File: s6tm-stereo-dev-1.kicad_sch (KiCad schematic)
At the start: 95 parts, among them J1 Micro_SD_Card_Det1, J2 Conn_01x04_Pin, J3 USB_C_Receptacle_USB2.0_14P, SW1 SW_SPDT, SW2 SW_Push, SW3 SW_Push, SW5 SW_Push, SW6 SW_Push, SW7 RotaryEncoder_Switch, U1 ESP32-S3FN8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

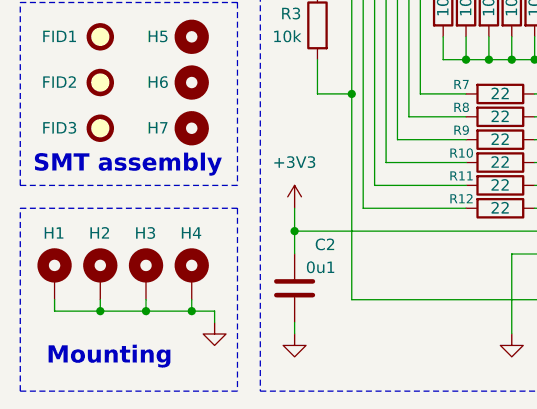
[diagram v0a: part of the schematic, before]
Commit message: schem/pcb: remove extra mounting hole
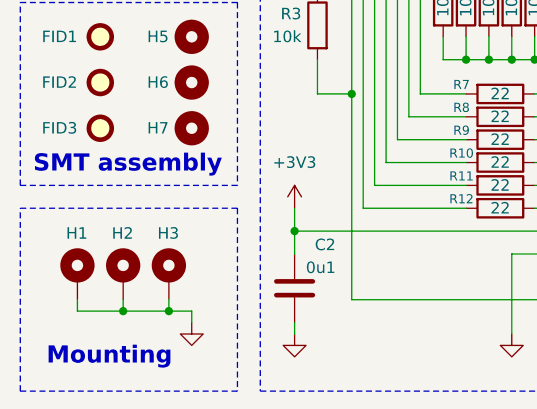
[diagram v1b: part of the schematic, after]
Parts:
- removed H4: MountingHole_Pad, MountingHole:MountingHole_3.2mm_M3_Pad_Via, symbol Mechanical:MountingHole_Pad
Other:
- moved on the sheet: H1, H2, H3
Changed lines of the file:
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@@
 	)
 	(junction
-		(at 29.21 185.42)
-		(diameter 0)
-		(color 0 0 0 0)
-	)
-	(junction
 		(at 64.77 157.48)
 		(diameter 0)
@@
 	)
 	(junction
-		(at 24.13 185.42)
-		(diameter 0)
-		(color 0 0 0 0)
-	)
-	(junction
 		(at 58.42 144.78)
 		(diameter 0)
@@
 	)
 	(junction
+		(at 31.75 185.42)
+		(diameter 0)
+		(color 0 0 0 0)
+	)
+	(junction
 		(at 153.67 180.34)
 		(diameter 0)
@@
 	)
 	(junction
-		(at 54.61 31.75)
+		(at 26.67 185.42)
 		(diameter 0)
 		(color 0 0 0 0)
 	)
 	(junction
-		(at 195.58 124.46)
+		(at 54.61 31.75)
 		(diameter 0)
 		(color 0 0 0 0)
 	)
 	(junction
-		(at 59.69 146.05)
+		(at 195.58 124.46)
 		(diameter 0)
 		(color 0 0 0 0)
 	)
 	(junction
-		(at 34.29 185.42)
+		(at 59.69 146.05)
 		(diameter 0)
 		(color 0 0 0 0)
@@
 	(wire
 		(pts
+			(xy 31.75 185.42) (xy 34.29 185.42)
+		)
+		(stroke
+			(width 0)
+			(type default)
+		)
+	)
+	(wire
+		(pts
 			(xy 67.31 143.51) (xy 57.15 143.51)
 		)
@@
 	(wire
 		(pts
-			(xy 19.05 185.42) (xy 24.13 185.42)
+			(xy 21.59 185.42) (xy 26.67 185.42)
 		)
 		(stroke
@@
 	(wire
 		(pts
-			(xy 19.05 185.42) (xy 19.05 184.15)
+			(xy 21.59 185.42) (xy 21.59 184.15)
 		)
 		(stroke
@@
 	(wire
 		(pts
-			(xy 29.21 185.42) (xy 29.21 184.15)
+			(xy 31.75 185.42) (xy 31.75 184.15)
 		)
 		(stroke
@@
 	(wire
 		(pts
-			(xy 34.29 185.42) (xy 34.29 184.15)
-		)
-		(stroke
-			(width 0)
-			(type default)
-		)
-	)
-	(wire
-		(pts
 			(xy 153.67 71.12) (xy 153.67 72.39)
 		)
@@
 	(wire
 		(pts
-			(xy 36.83 185.42) (xy 34.29 185.42)
-		)
-		(stroke
-			(width 0)
-			(type default)
-		)
-	)
-	(wire
-		(pts
 			(xy 77.47 21.59) (xy 78.74 21.59)
 		)
@@
 	(wire
 		(pts
-			(xy 24.13 185.42) (xy 29.21 185.42)
-		)
-		(stroke
-			(width 0)
-			(type default)
-		)
-	)
-	(wire
-		(pts
 			(xy 72.39 154.94) (xy 72.39 157.48)
 		)
@@
 	(wire
 		(pts
+			(xy 26.67 185.42) (xy 31.75 185.42)
+		)
+		(stroke
+			(width 0)
+			(type default)
+		)
+	)
+	(wire
+		(pts
 			(xy 195.58 119.38) (xy 195.58 124.46)
 		)
@@
 	(wire
 		(pts
-			(xy 29.21 185.42) (xy 34.29 185.42)
-		)
-		(stroke
-			(width 0)
-			(type default)
-		)
-	)
-	(wire
-		(pts
 			(xy 250.19 147.32) (xy 252.73 147.32)
 		)
@@
 	(wire
 		(pts
-			(xy 36.83 185.42) (xy 36.83 186.69)
+			(xy 34.29 185.42) (xy 34.29 186.69)
 		)
 		(stroke
@@
 	(wire
 		(pts
-			(xy 24.13 185.42) (xy 24.13 184.15)
+			(xy 26.67 185.42) (xy 26.67 184.15)
 		)
 		(stroke
@@
 	(symbol
 		(lib_id "Mechanical:MountingHole_Pad")
-		(at 29.21 181.61 0)
+		(at 31.75 181.61 0)
 		(unit 1)
 		(body_style 1)
@@
 		(dnp no)
 		(property "Reference" "H3"
-			(at 27.94 176.784 0)
+			(at 30.48 176.784 0)
 			(show_name no)
 			(do_not_autoplace no)
@@
 		)
 		(property "Value" "MountingHole_Pad"
-			(at 33.02 180.34 90)
+			(at 35.56 180.34 90)
 			(hide yes)
 			(show_name no)
@@
 		)
 		(property "Footprint" "MountingHole:MountingHole_3.2mm_M3_Pad_Via"
-			(at 29.21 181.61 0)
+			(at 31.75 181.61 0)
 			(hide yes)
 			(show_name no)
@@
 		)
 		(property "Datasheet" ""
-			(at 29.21 181.61 0)
+			(at 31.75 181.61 0)
 			(hide yes)
 			(show_name no)
@@
 		)
 		(property "Description" "Mounting Hole with connection"
-			(at 29.21 181.61 0)
+			(at 31.75 181.61 0)
 			(hide yes)
 			(show_name no)
@@
 	(symbol
 		(lib_id "power:GND")
-		(at 36.83 186.69 0)
+		(at 34.29 186.69 0)
 		(unit 1)
 		(body_style 1)
@@
 		(dnp no)
 		(property "Reference" "#PWR0126"
-			(at 36.83 193.04 0)
+			(at 34.29 193.04 0)
 			(hide yes)
 			(show_name no)
@@
 		)
 		(property "Value" "GND"
-			(at 36.576 191.262 0)
+			(at 34.036 191.262 0)
 			(hide yes)
 			(show_name no)
@@
 		)
 		(property "Footprint" ""
-			(at 36.83 186.69 0)
+			(at 34.29 186.69 0)
 			(hide yes)
 			(show_name no)
@@
 		)
 		(property "Datasheet" ""
-			(at 36.83 186.69 0)
+			(at 34.29 186.69 0)
 			(hide yes)
 			(show_name no)
@@
 		)
 		(property "Description" "Power symbol creates a global label with name \"GND\" , ground"
-			(at 36.83 186.69 0)
+			(at 34.29 186.69 0)
 			(hide yes)
 			(show_name no)
@@
 	)
 	(symbol
-		(lib_id "Mechanical:MountingHole_Pad")
-		(at 34.29 181.61 0)
-		(unit 1)
-		(body_style 1)
-		(exclude_from_sim no)
-		(in_bom no)
-		(on_board yes)
-		(in_pos_files yes)
-		(dnp no)
-		(property "Reference" "H4"
-			(at 33.02 176.784 0)
-			(show_name no)
-			(do_not_autoplace no)
-			(effects
-				(font
-					(size 1.27 1.27)
-				)
-				(justify left)
-			)
-		)
-		(property "Value" "MountingHole_Pad"
-			(at 38.1 180.34 90)
-			(hide yes)
-			(show_name no)
-			(do_not_autoplace no)
-			(effects
-				(font
-					(size 1.27 1.27)
-				)
-			)
-		)
-		(property "Footprint" "MountingHole:MountingHole_3.2mm_M3_Pad_Via"
-			(at 34.29 181.61 0)
-			(hide yes)
-			(show_name no)
-			(do_not_autoplace no)
-			(effects
-				(font
-					(size 1.27 1.27)
-				)
-			)
-		)
-		(property "Datasheet" ""
-			(at 34.29 181.61 0)
-			(hide yes)
-			(show_name no)
-			(do_not_autoplace no)
-			(effects
-				(font
-					(size 1.27 1.27)
-				)
-			)
-		)
-		(property "Description" "Mounting Hole with connection"
-			(at 34.29 181.61 0)
-			(hide yes)
-			(show_name no)
-			(do_not_autoplace no)
-			(effects
-				(font
-					(size 1.27 1.27)
-				)
-			)
-		)
-		(pin "1"
-		)
-		(instances
-			(project "s6tm-stereo-dev-1"
-				(path "/41fad0d7-0cae-453e-a16c-bdf8be036e99"
-					(reference "H4")
-					(unit 1)
-				)
-			)
-		)
-	)
-	(symbol
 		(lib_id "Device:D_Schottky")
 		(at 270.51 127 0)
@@
 	(symbol
 		(lib_id "Mechanical:MountingHole_Pad")
-		(at 24.13 181.61 0)
+		(at 26.67 181.61 0)
 		(unit 1)
 		(body_style 1)
@@
 		(dnp no)
 		(property "Reference" "H2"
-			(at 22.86 176.784 0)
+			(at 25.4 176.784 0)
 			(show_name no)
 			(do_not_autoplace no)
@@
 		)
 		(property "Value" "MountingHole_Pad"
-			(at 27.94 180.34 90)
+			(at 30.48 180.34 90)
 			(hide yes)
 			(show_name no)
@@
 		)
 		(property "Footprint" "MountingHole:MountingHole_3.2mm_M3_Pad_Via"
-			(at 24.13 181.61 0)
+			(at 26.67 181.61 0)
 			(hide yes)
 			(show_name no)
@@
 		)
 		(property "Datasheet" ""
-			(at 24.13 181.61 0)
+			(at 26.67 181.61 0)
 			(hide yes)
 			(show_name no)
@@
 		)
 		(property "Description" "Mounting Hole with connection"
-			(at 24.13 181.61 0)
+			(at 26.67 181.61 0)
 			(hide yes)
 			(show_name no)
@@
 	(symbol
 		(lib_id "Mechanical:MountingHole_Pad")
-		(at 19.05 181.61 0)
+		(at 21.59 181.61 0)
 		(unit 1)
 		(body_style 1)
@@
 		(dnp no)
 		(property "Reference" "H1"
-			(at 17.78 176.784 0)
+			(at 20.32 176.784 0)
 			(show_name no)
 			(do_not_autoplace no)
@@
 		)
 		(property "Value" "MountingHole_Pad"
-			(at 22.86 180.34 90)
+			(at 25.4 180.34 90)
 			(hide yes)
 			(show_name no)
@@
 		)
 		(property "Footprint" "MountingHole:MountingHole_3.2mm_M3_Pad_Via"
-			(at 19.05 181.61 0)
+			(at 21.59 181.61 0)
 			(hide yes)
 			(show_name no)
@@
 		)
 		(property "Datasheet" ""
-			(at 19.05 181.61 0)
+			(at 21.59 181.61 0)
 			(hide yes)
 			(show_name no)
@@
 		)
 		(property "Description" "Mounting Hole with connection"
-			(at 19.05 181.61 0)
+			(at 21.59 181.61 0)
 			(hide yes)
 			(show_name no)

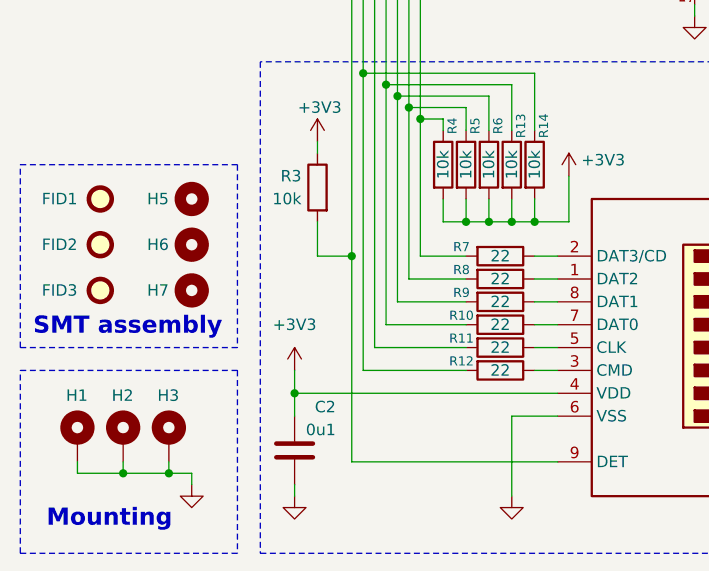
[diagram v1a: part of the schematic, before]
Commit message: pcb: refine sd layout
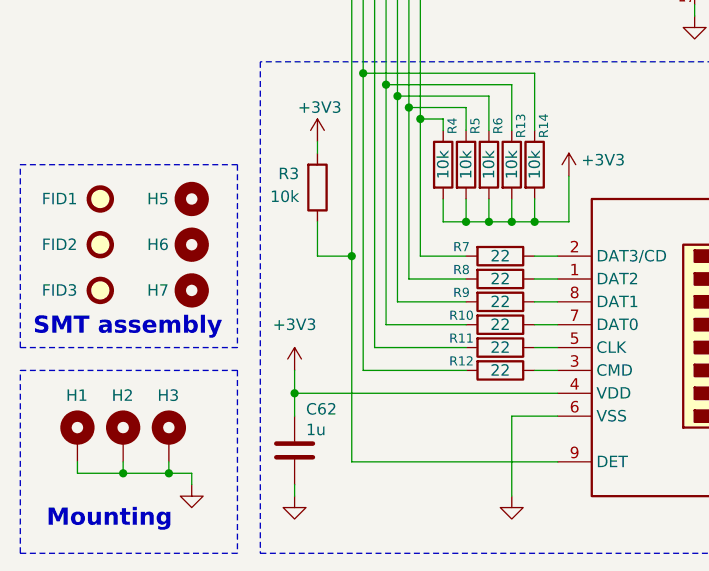
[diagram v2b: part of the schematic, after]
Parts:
- removed C2: 0u1, Capacitor_SMD:C_0603_1608Metric, symbol Device:C
- added C62: 1u, Capacitor_SMD:C_0402_1005Metric, symbol Device:C
- R3: footprint Resistor_SMD:R_0603_1608Metric -> Resistor_SMD:R_0402_1005Metric; JLCPCB Part # C25804 -> C25744; Manufacturer Part Number 0603WAF1002T5E -> 0402WGF1002TCE
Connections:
- net +3V3: now also R3.2, C62.1; no longer R3.1
- net GND: now also C62.2
- net at J1.9 (DET), U1.36 (SPICLK_N/GPIO48): now also R3.1; no longer R3.2

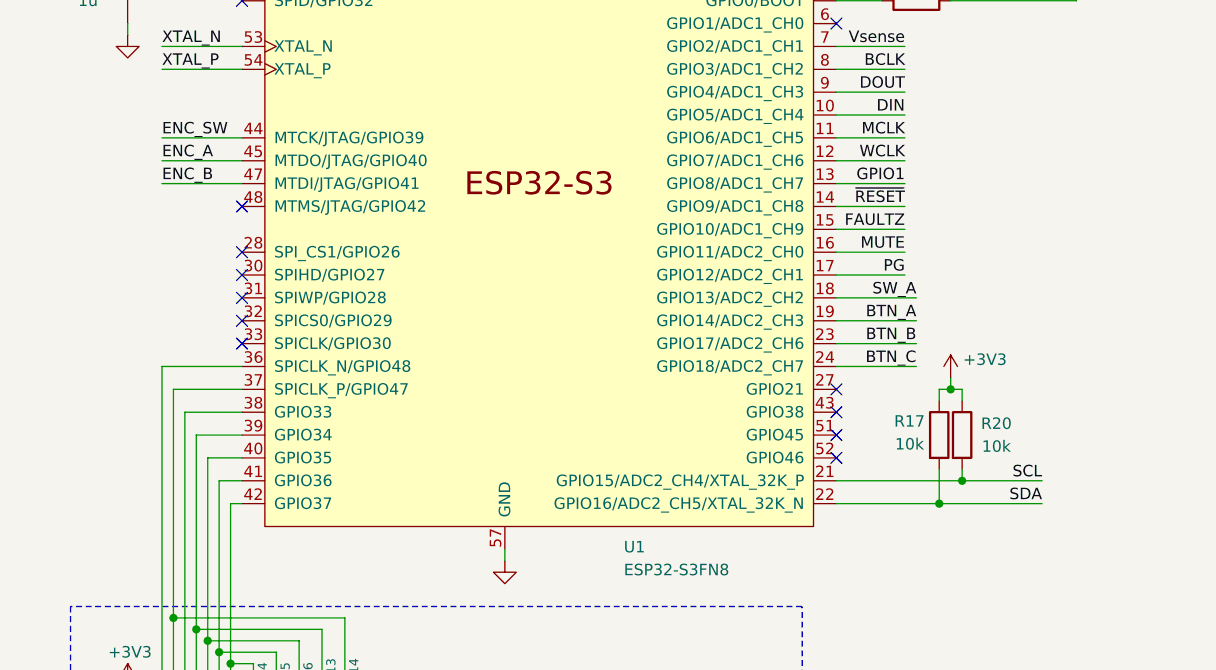
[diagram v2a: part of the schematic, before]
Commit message: pcb: add HSE xtal routing
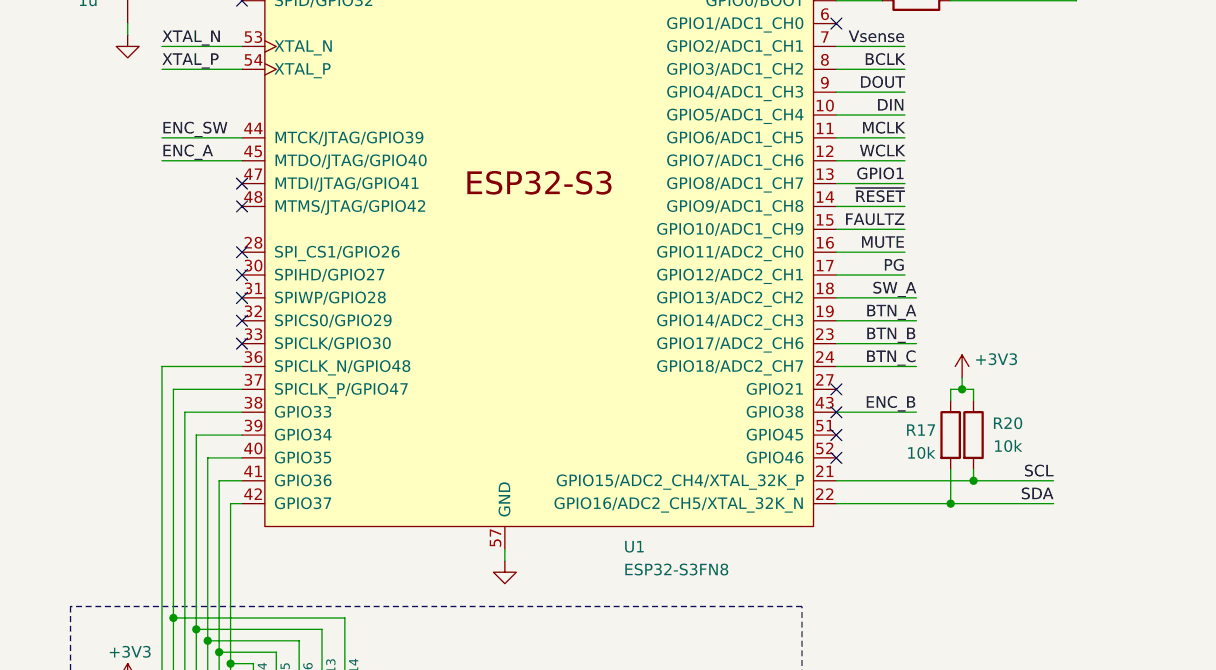
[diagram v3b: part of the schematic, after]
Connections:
- net ENC_B: now also U1.43 (GPIO38); no longer U1.47 (MTDI/JTAG/GPIO41)
- no-connect marks 13 -> 14
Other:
- moved on the sheet: R17, R20
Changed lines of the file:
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@@
 	)
 	(junction
-		(at 138.43 128.27)
+		(at 139.7 128.27)
 		(diameter 0)
 		(color 0 0 0 0)
@@
 	)
 	(junction
-		(at 140.97 125.73)
+		(at 142.24 125.73)
 		(diameter 0)
 		(color 0 0 0 0)
@@
 	)
 	(junction
-		(at 139.7 115.57)
+		(at 140.97 115.57)
 		(diameter 0)
 		(color 0 0 0 0)
@@
 	)
 	(no_connect
+		(at 60.96 92.71)
+	)
+	(no_connect
 		(at 127 115.57)
 	)
@@
 	(wire
 		(pts
-			(xy 139.7 114.3) (xy 139.7 115.57)
+			(xy 140.97 114.3) (xy 140.97 115.57)
 		)
 		(stroke
@@
 	(wire
 		(pts
-			(xy 127 128.27) (xy 138.43 128.27)
-		)
-		(stroke
-			(width 0)
-			(type default)
-		)
-	)
-	(wire
-		(pts
 			(xy 266.7 127) (xy 265.43 127)
 		)
@@
 	(wire
 		(pts
-			(xy 140.97 115.57) (xy 139.7 115.57)
+			(xy 142.24 115.57) (xy 140.97 115.57)
 		)
 		(stroke
@@
 	(wire
 		(pts
-			(xy 127 125.73) (xy 140.97 125.73)
-		)
-		(stroke
-			(width 0)
-			(type default)
-		)
-	)
-	(wire
-		(pts
 			(xy 52.07 113.03) (xy 52.07 161.29)
 		)
@@
 	(wire
 		(pts
+			(xy 127 125.73) (xy 142.24 125.73)
+		)
+		(stroke
+			(width 0)
+			(type default)
+		)
+	)
+	(wire
+		(pts
 			(xy 60.96 115.57) (xy 53.34 115.57)
 		)
@@
 	(wire
 		(pts
-			(xy 52.07 92.71) (xy 60.96 92.71)
-		)
-		(stroke
-			(width 0)
-			(type default)
-		)
-	)
-	(wire
-		(pts
 			(xy 251.46 153.67) (xy 254 153.67)
 		)
@@
 	(wire
 		(pts
-			(xy 138.43 124.46) (xy 138.43 128.27)
+			(xy 139.7 124.46) (xy 139.7 128.27)
 		)
 		(stroke
@@
 	(wire
 		(pts
-			(xy 140.97 116.84) (xy 140.97 115.57)
+			(xy 142.24 116.84) (xy 142.24 115.57)
 		)
 		(stroke
@@
 	(wire
 		(pts
-			(xy 138.43 116.84) (xy 138.43 115.57)
+			(xy 139.7 116.84) (xy 139.7 115.57)
 		)
 		(stroke
@@
 	(wire
 		(pts
-			(xy 138.43 115.57) (xy 139.7 115.57)
+			(xy 139.7 115.57) (xy 140.97 115.57)
 		)
 		(stroke
@@
 	(wire
 		(pts
-			(xy 140.97 125.73) (xy 149.86 125.73)
+			(xy 142.24 125.73) (xy 151.13 125.73)
 		)
 		(stroke
@@
 	(wire
 		(pts
-			(xy 138.43 128.27) (xy 149.86 128.27)
+			(xy 139.7 128.27) (xy 151.13 128.27)
 		)
 		(stroke
@@
 	(wire
 		(pts
+			(xy 127 128.27) (xy 139.7 128.27)
+		)
+		(stroke
+			(width 0)
+			(type default)
+		)
+	)
+	(wire
+		(pts
 			(xy 173.99 59.69) (xy 181.61 59.69)
 		)
@@
 	(wire
 		(pts
+			(xy 135.89 118.11) (xy 127 118.11)
+		)
+		(stroke
+			(width 0)
+			(type default)
+		)
+	)
+	(wire
+		(pts
 			(xy 68.58 30.48) (xy 68.58 31.75)
 		)
@@
 	(wire
 		(pts
-			(xy 140.97 124.46) (xy 140.97 125.73)
+			(xy 142.24 124.46) (xy 142.24 125.73)
 		)
 		(stroke
@@
 	)
 	(label "SDA"
-		(at 149.86 128.27 180)
+		(at 151.13 128.27 180)
 		(effects
 			(font
@@
 	)
 	(label "SCL"
-		(at 149.86 125.73 180)
+		(at 151.13 125.73 180)
 		(effects
 			(font
@@
 		)
 	)
-	(label "ENC_B"
-		(at 52.07 92.71 0)
-		(effects
-			(font
-				(size 1.27 1.27)
-			)
-			(justify left bottom)
-		)
-	)
 	(label "XTAL_P"
 		(at 52.07 80.01 0)
@@
 		)
 	)
+	(label "ENC_B"
+		(at 135.89 118.11 180)
+		(effects
+			(font
+				(size 1.27 1.27)
+			)
+			(justify right bottom)
+		)
+	)
 	(label "MUTE"
 		(at 222.25 41.91 180)
@@
 	(symbol
 		(lib_id "Device:R")
-		(at 140.97 120.65 0)
+		(at 142.24 120.65 0)
 		(unit 1)
 		(body_style 1)
@@
 		(dnp no)
 		(property "Reference" "R20"
-			(at 144.78 119.38 0)
+			(at 146.05 119.38 0)
 			(show_name no)
 			(do_not_autoplace no)
@@
 		)
 		(property "Value" "10k"
-			(at 144.78 121.92 0)
+			(at 146.05 121.92 0)
 			(show_name no)
 			(do_not_autoplace no)
@@
 		)
 		(property "Footprint" "Resistor_SMD:R_0402_1005Metric"
-			(at 139.192 120.65 90)
+			(at 140.462 120.65 90)
 			(hide yes)
 			(show_name no)
@@
 		)
 		(property "Datasheet" ""
-			(at 140.97 120.65 0)
+			(at 142.24 120.65 0)
 			(hide yes)
 			(show_name no)
@@
 		)
 		(property "Description" "Resistor"
-			(at 140.97 120.65 0)
+			(at 142.24 120.65 0)
 			(hide yes)
 			(show_name no)
@@
 		)
 		(property "Basic" "Y"
-			(at 140.97 120.65 90)
+			(at 142.24 120.65 90)
 			(hide yes)
 			(show_name no)
@@
 		)
 		(property "JLCPCB Part #" "C25744"
-			(at 140.97 120.65 90)
+			(at 142.24 120.65 90)
 			(hide yes)
 			(show_name no)
@@
 		)
 		(property "Manufacturer" "Uniroyal Elec"
-			(at 140.97 120.65 90)
+			(at 142.24 120.65 90)
 			(hide yes)
 			(show_name no)
@@
 		)
 		(property "Manufacturer Part Number" "0402WGF1002TCE"
-			(at 140.97 120.65 90)
+			(at 142.24 120.65 90)
 			(hide yes)
 			(show_name no)
@@
 	(symbol
 		(lib_id "Device:R")
-		(at 138.43 120.65 0)
+		(at 139.7 120.65 0)
 		(unit 1)
 		(body_style 1)
@@
 		(dnp no)
 		(property "Reference" "R17"
-			(at 135.128 119.126 0)
+			(at 136.398 120.142 0)
 			(show_name no)
 			(do_not_autoplace no)
@@
 		)
 		(property "Value" "10k"
-			(at 135.128 121.666 0)
+			(at 136.398 122.682 0)
 			(show_name no)
 			(do_not_autoplace no)
@@
 		)
 		(property "Footprint" "Resistor_SMD:R_0402_1005Metric"
-			(at 136.652 120.65 90)
+			(at 137.922 120.65 90)
 			(hide yes)
 			(show_name no)
@@
 		)
 		(property "Datasheet" ""
-			(at 138.43 120.65 0)
+			(at 139.7 120.65 0)
 			(hide yes)
 			(show_name no)
@@
 		)
 		(property "Description" "Resistor"
-			(at 138.43 120.65 0)
+			(at 139.7 120.65 0)
 			(hide yes)
 			(show_name no)
@@
 		)
 		(property "Basic" "Y"
-			(at 138.43 120.65 90)
+			(at 139.7 120.65 90)
 			(hide yes)
 			(show_name no)
@@
 		)
 		(property "JLCPCB Part #" "C25744"
-			(at 138.43 120.65 90)
+			(at 139.7 120.65 90)
 			(hide yes)
 			(show_name no)
@@
 		)
 		(property "Manufacturer" "Uniroyal Elec"
-			(at 138.43 120.65 90)
+			(at 139.7 120.65 90)
 			(hide yes)
 			(show_name no)
@@
 		)
 		(property "Manufacturer Part Number" "0402WGF1002TCE"
-			(at 138.43 120.65 90)
+			(at 139.7 120.65 90)
 			(hide yes)
 			(show_name no)
@@
 	(symbol
 		(lib_id "power:+3V3")
-		(at 139.7 114.3 0)
+		(at 140.97 114.3 0)
 		(unit 1)
 		(body_style 1)
@@
 		(dnp no)
 		(property "Reference" "#PWR023"
-			(at 139.7 118.11 0)
+			(at 140.97 118.11 0)
 			(hide yes)
 			(show_name no)
@@
 		)
 		(property "Value" "+3V3"
-			(at 143.51 112.268 0)
+			(at 144.78 112.268 0)
 			(show_name no)
 			(do_not_autoplace no)
@@
 		)
 		(property "Footprint" ""
-			(at 139.7 114.3 0)
+			(at 140.97 114.3 0)
 			(hide yes)
 			(show_name no)
@@
 		)
 		(property "Datasheet" ""
-			(at 139.7 114.3 0)
+			(at 140.97 114.3 0)
 			(hide yes)
 			(show_name no)
@@
 		)
 		(property "Description" "Power symbol creates a global label with name \"+3V3\""
-			(at 139.7 114.3 0)
+			(at 140.97 114.3 0)
 			(hide yes)
 			(show_name no)
